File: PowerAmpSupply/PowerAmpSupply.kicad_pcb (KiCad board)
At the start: 4 copper layers, 80.5 x 40 mm, 116 parts, among them J1 VIN_BRIDGE, J2 VIN_BRIDGE, J3 GND_BRIDGE, J4 GND_BRIDGE, J5 VIN, J6 VOUT, J7 VTRK_EXT, M1 12V 6Vstart <100mA, Q1 EPC2306, Q2 PNP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

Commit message: PowerAmp+Supply fan LDO change, Supply Rgate fix
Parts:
- R7, R8: value 1Ω -> 3.3Ω
- U3: value AP2202-ADJ -> TPS7A2401
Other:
- board text added: "Modular Audio Power Amp Supply v1.1"
- board text removed: "Modular Audio Power Amp Supply"

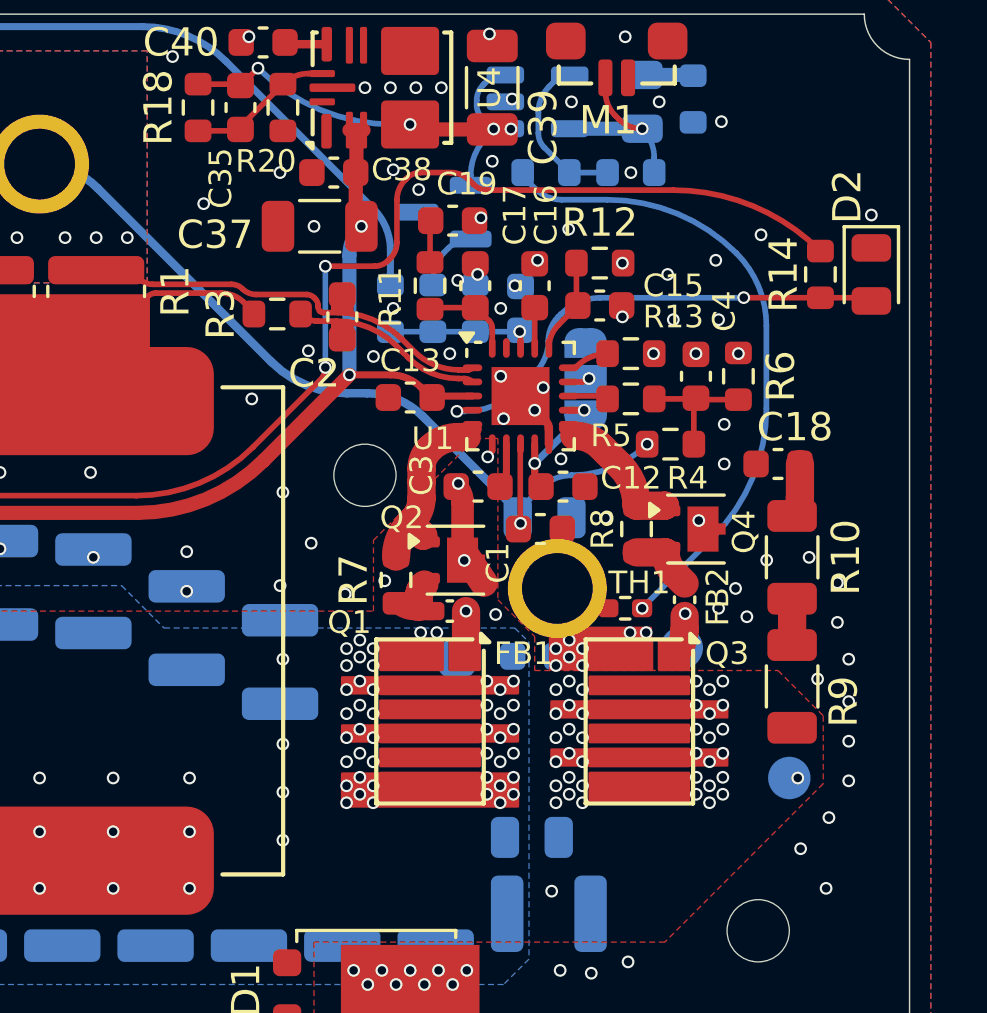
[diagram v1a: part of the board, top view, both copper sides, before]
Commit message: PowerAmpSupply coax test connectors
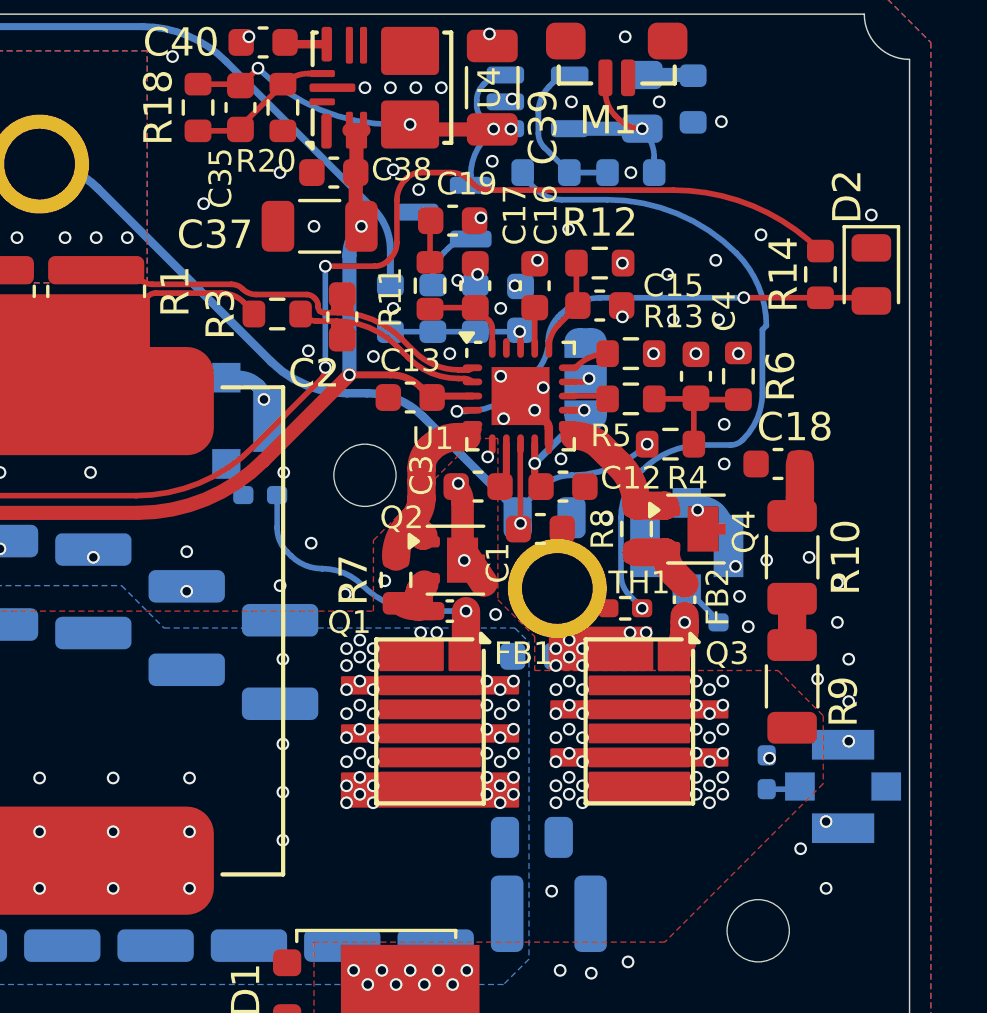
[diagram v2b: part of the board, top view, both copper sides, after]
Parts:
- removed TP1: SW, TestPoint:TestPoint_Pad_D1.5mm
- removed TP2: HO, TestPoint:TestPoint_Pad_D1.5mm
- removed TP3: LO, TestPoint:TestPoint_Pad_D1.5mm
- added J10: SW, BW_Connectors:TE_CONMHF1-SMD, B.Cu at (187.9, 107.3)
- added J8: LO, BW_Connectors:TE_CONMHF1-SMD, B.Cu at (182.4, 98.8)
- added J9: HO, BW_Connectors:TE_CONMHF1-SMD, B.Cu at (166.1, 94.4)
- added R32: 50Ω, Resistor_SMD:R_0402_1005Metric_Pad0.72x0.64mm_HandSolder, B.Cu at (167.3, 97.0)
- added R33: 50Ω, Resistor_SMD:R_0402_1005Metric_Pad0.72x0.64mm_HandSolder, B.Cu at (185.2, 106.8)
- added R34: 50Ω, Resistor_SMD:R_0402_1005Metric_Pad0.72x0.64mm_HandSolder, B.Cu at (182.9, 101.5)
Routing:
- net GND: track 6.53 -> 16.7 mm, vias 132 -> 131
- net Net-(Q1-G): track 3.35 -> 10.5 mm
- net Net-(R21-Pad2): track 22.7 -> 24.7 mm
- net Net-(J8-In): track 0.00 -> 1.63 mm
- net Net-(J9-In): track 0.00 -> 1.29 mm
- net Net-(Q3-G): track 2.71 -> 1.47 mm
- net Net-(J10-In): track 0.00 -> 1.20 mm

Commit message: PowerAmpSupply VTRK change
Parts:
- R15: value 28kΩ 0.1% -> 84.5kΩ 0.1%
- R16: value 28kΩ 0.1% -> 42.2kΩ 0.1%

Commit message: PowerAmpSupply adjusted max VIN to 24V
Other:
- board text added: "INPUT 11-24V 40A max"
- board text removed: "INPUT 11-22V 40A max"

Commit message: PowerAmpSupply UVLO increase
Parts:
- R6: value 8.87kΩ -> 10kΩ

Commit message: PowerAmpSupply slower inrush applied and tested
Seems to work, so included the change in the design
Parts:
- R25: value 13kΩ -> 30kΩ
